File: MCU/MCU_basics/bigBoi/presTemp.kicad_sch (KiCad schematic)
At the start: 3 parts, among them J3 DM3AT-SF-PEJM5_40_

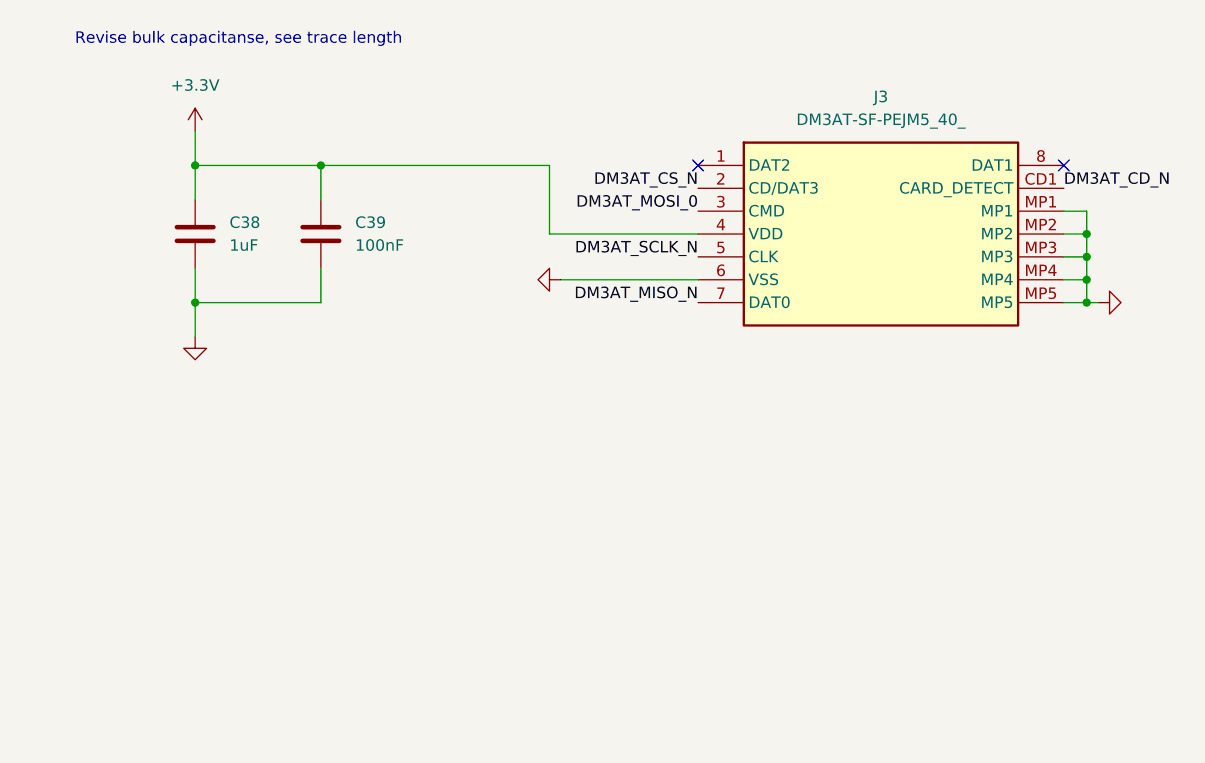
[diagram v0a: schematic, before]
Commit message: schematic connections
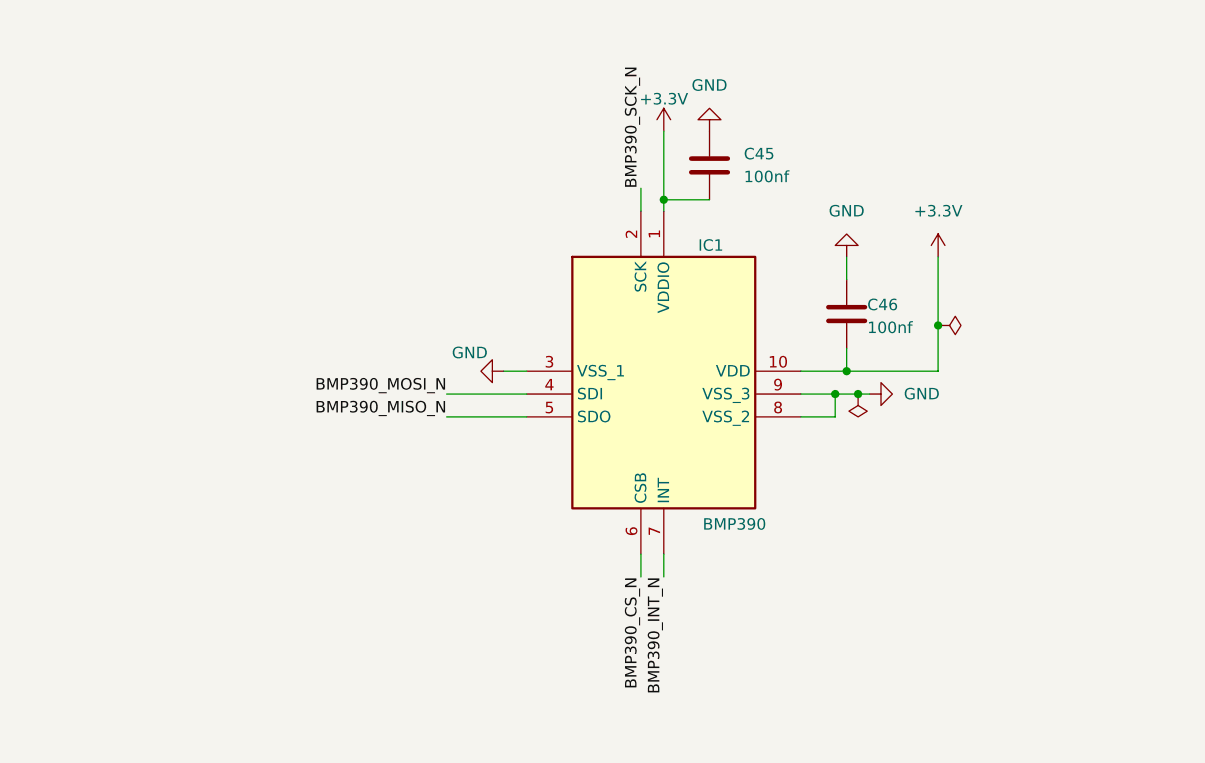
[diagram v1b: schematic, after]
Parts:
- removed C38: 1uF, symbol Device:C
- removed C39: 100nF, symbol Device:C
- removed J3: DM3AT-SF-PEJM5_40_, DM3ATSFPEJM540, symbol DM3AT:DM3AT-SF-PEJM5_40_
- added C45, C46: 100nf, Capacitor_SMD:C_0402_1005Metric, symbol Device:C
- added IC1: BMP390, BMP390:BMP390, symbol BMP390:BMP390
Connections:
- net +3.3V: now also C45.2, C46.2, IC1.1 (VDDIO), IC1.10 (VDD)
- new net BMP390_CS_N: IC1.6 (CSB)
- new net BMP390_INT_N: IC1.7 (INT)
- new net BMP390_MISO_N: IC1.5 (SDO)
- new net BMP390_MOSI_N: IC1.4 (SDI)
- new net BMP390_SCK_N: IC1.2 (SCK)
- new net GND: C45.1, C46.1, IC1.3 (VSS_1), IC1.8 (VSS_2), IC1.9 (VSS_3)
- no-connect marks 2 -> 0
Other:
- note removed: "Revise bulk capacitanse, see trace length"

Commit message: ERC resolving
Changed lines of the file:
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@@
 	(paper "A4")
-	(junction
-		(at 176.53 105.41)
-		(diameter 0)
-		(color 0 0 0 0)
-	)
 	(junction
 		(at 165.1 113.03)
@@
 		(color 0 0 0 0)
 	)
-	(junction
-		(at 167.64 113.03)
-		(diameter 0)
-		(color 0 0 0 0)
-	)
 	(wire
 		(pts
@@
 	(wire
 		(pts
-			(xy 176.53 105.41) (xy 176.53 110.49)
-		)
-		(stroke
-			(width 0)
-			(type default)
-		)
-	)
-	(wire
-		(pts
-			(xy 167.64 113.03) (xy 168.91 113.03)
+			(xy 176.53 97.79) (xy 176.53 110.49)
+		)
+		(stroke
+			(width 0)
+			(type default)
+		)
+	)
+	(wire
+		(pts
+			(xy 165.1 113.03) (xy 168.91 113.03)
 		)
 		(stroke
@@
 	(wire
 		(pts
-			(xy 165.1 113.03) (xy 167.64 113.03)
-		)
-		(stroke
-			(width 0)
-			(type default)
-		)
-	)
-	(wire
-		(pts
 			(xy 166.37 97.79) (xy 166.37 100.33)
 		)
@@
 	(wire
 		(pts
-			(xy 176.53 97.79) (xy 176.53 105.41)
-		)
-		(stroke
-			(width 0)
-			(type default)
-		)
-	)
-	(wire
-		(pts
 			(xy 161.29 110.49) (xy 166.37 110.49)
 		)
@@
 		)
 	)
-	(label "BMP390_SCK_N"
+	(global_label "BMP390_SCK_N"
+		(shape input)
 		(at 143.51 90.17 90)
-		(effects
-			(font
-				(size 1.27 1.27)
-			)
-			(justify left bottom)
-		)
-	)
-	(label "BMP390_INT_N"
+		(fields_autoplaced yes)
+		(effects
+			(font
+				(size 1.27 1.27)
+			)
+			(justify left)
+		)
+		(property "Intersheetrefs" "${INTERSHEET_REFS}"
+			(at 143.51 72.5497 90)
+			(hide yes)
+			(show_name no)
+			(do_not_autoplace no)
+			(effects
+				(font
+					(size 1.27 1.27)
+				)
+				(justify left)
+			)
+		)
+	)
+	(global_label "BMP390_MOSI_N"
+		(shape input)
+		(at 121.92 113.03 180)
+		(fields_autoplaced yes)
+		(effects
+			(font
+				(size 1.27 1.27)
+			)
+			(justify right)
+		)
+		(property "Intersheetrefs" "${INTERSHEET_REFS}"
+			(at 103.453 113.03 0)
+			(hide yes)
+			(show_name no)
+			(do_not_autoplace no)
+			(effects
+				(font
+					(size 1.27 1.27)
+				)
+				(justify right)
+			)
+		)
+	)
+	(global_label "BMP390_INT_N"
+		(shape input)
 		(at 146.05 133.35 270)
-		(effects
-			(font
-				(size 1.27 1.27)
-			)
-			(justify right bottom)
-		)
-	)
-	(label "BMP390_CS_N"
+		(fields_autoplaced yes)
+		(effects
+			(font
+				(size 1.27 1.27)
+			)
+			(justify right)
+		)
+		(property "Intersheetrefs" "${INTERSHEET_REFS}"
+			(at 146.05 150.1237 90)
+			(hide yes)
+			(show_name no)
+			(do_not_autoplace no)
+			(effects
+				(font
+					(size 1.27 1.27)
+				)
+				(justify right)
+			)
+		)
+	)
+	(global_label "BMP390_MISO_N"
+		(shape input)
+		(at 121.92 115.57 180)
+		(fields_autoplaced yes)
+		(effects
+			(font
+				(size 1.27 1.27)
+			)
+			(justify right)
+		)
+		(property "Intersheetrefs" "${INTERSHEET_REFS}"
+			(at 103.453 115.57 0)
+			(hide yes)
+			(show_name no)
+			(do_not_autoplace no)
+			(effects
+				(font
+					(size 1.27 1.27)
+				)
+				(justify right)
+			)
+		)
+	)
+	(global_label "BMP390_CS_N"
+		(shape input)
 		(at 143.51 133.35 270)
-		(effects
-			(font
-				(size 1.27 1.27)
-			)
-			(justify right bottom)
-		)
-	)
-	(label "BMP390_MISO_N"
-		(at 121.92 115.57 180)
-		(effects
-			(font
-				(size 1.27 1.27)
-			)
-			(justify right bottom)
-		)
-	)
-	(label "BMP390_MOSI_N"
-		(at 121.92 113.03 180)
-		(effects
-			(font
-				(size 1.27 1.27)
-			)
-			(justify right bottom)
-		)
-	)
-	(symbol
-		(lib_id "power:PWR_FLAG")
-		(at 176.53 105.41 270)
-		(unit 1)
-		(body_style 1)
-		(exclude_from_sim no)
-		(in_bom yes)
-		(on_board yes)
-		(in_pos_files yes)
-		(dnp no)
-		(fields_autoplaced yes)
-		(property "Reference" "#FLG06"
-			(at 178.435 105.41 0)
-			(hide yes)
-			(show_name no)
-			(do_not_autoplace no)
-			(effects
-				(font
-					(size 1.27 1.27)
-				)
-			)
-		)
-		(property "Value" "PWR_FLAG"
-			(at 180.34 105.4099 90)
-			(hide yes)
-			(show_name no)
-			(do_not_autoplace no)
-			(effects
-				(font
-					(size 1.27 1.27)
-				)
-				(justify left)
-			)
-		)
-		(property "Footprint" ""
-			(at 176.53 105.41 0)
-			(hide yes)
-			(show_name no)
-			(do_not_autoplace no)
-			(effects
-				(font
-					(size 1.27 1.27)
-				)
-			)
-		)
-		(property "Datasheet" ""
-			(at 176.53 105.41 0)
-			(hide yes)
-			(show_name no)
-			(do_not_autoplace no)
-			(effects
-				(font
-					(size 1.27 1.27)
-				)
-			)
-		)
-		(property "Description" "Special symbol for telling ERC where power comes from"
-			(at 176.53 105.41 0)
-			(hide yes)
-			(show_name no)
-			(do_not_autoplace no)
-			(effects
-				(font
-					(size 1.27 1.27)
-				)
-			)
-		)
-		(pin "1"
-		)
-		(instances
-			(project "bigBoi"
-				(path "/0a118c22-2522-42a6-b7a6-70c79326ece4/7e17ce98-d5ff-4274-a7f7-9b15cee26061"
-					(reference "#FLG06")
-					(unit 1)
-				)
+		(fields_autoplaced yes)
+		(effects
+			(font
+				(size 1.27 1.27)
+			)
+			(justify right)
+		)
+		(property "Intersheetrefs" "${INTERSHEET_REFS}"
+			(at 143.51 149.7003 90)
+			(hide yes)
+			(show_name no)
+			(do_not_autoplace no)
+			(effects
+				(font
+					(size 1.27 1.27)
+				)
+				(justify right)
 			)
 		)
@@
 					(unit 1)
 				)
-			)
-		)
-	)
-	(symbol
-		(lib_id "power:PWR_FLAG")
-		(at 167.64 113.03 180)
-		(unit 1)
-		(body_style 1)
-		(exclude_from_sim no)
-		(in_bom yes)
-		(on_board yes)
-		(in_pos_files yes)
-		(dnp no)
-		(fields_autoplaced yes)
-		(property "Reference" "#FLG05"
-			(at 167.64 114.935 0)
-			(hide yes)
-			(show_name no)
-			(do_not_autoplace no)
-			(effects
-				(font
-					(size 1.27 1.27)
-				)
-			)
-		)
-		(property "Value" "PWR_FLAG"
-			(at 167.64 118.11 0)
-			(hide yes)
-			(show_name no)
-			(do_not_autoplace no)
-			(effects
-				(font
-					(size 1.27 1.27)
-				)
-			)
-		)
-		(property "Footprint" ""
-			(at 167.64 113.03 0)
-			(hide yes)
-			(show_name no)
-			(do_not_autoplace no)
-			(effects
-				(font
-					(size 1.27 1.27)
-				)
-			)
-		)
-		(property "Datasheet" ""
-			(at 167.64 113.03 0)
-			(hide yes)
-			(show_name no)
-			(do_not_autoplace no)
-			(effects
-				(font
-					(size 1.27 1.27)
-				)
-			)
-		)
-		(property "Description" "Special symbol for telling ERC where power comes from"
-			(at 167.64 113.03 0)
-			(hide yes)
-			(show_name no)
-			(do_not_autoplace no)
-			(effects
-				(font
-					(size 1.27 1.27)
-				)
-			)
-		)
-		(pin "1"
-		)
-		(instances
-			(project "bigBoi"
-				(path "/0a118c22-2522-42a6-b7a6-70c79326ece4/7e17ce98-d5ff-4274-a7f7-9b15cee26061"
-					(reference "#FLG05")
-					(unit 1)
-				)
